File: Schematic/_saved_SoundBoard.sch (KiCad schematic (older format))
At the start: 0 parts

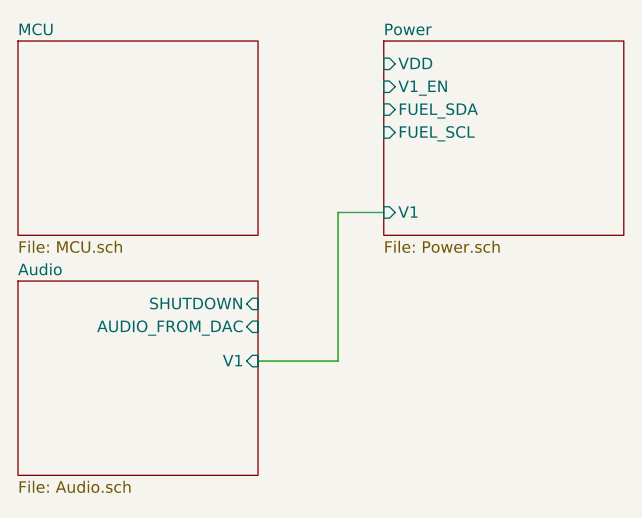
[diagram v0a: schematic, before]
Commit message: Add power circuitry
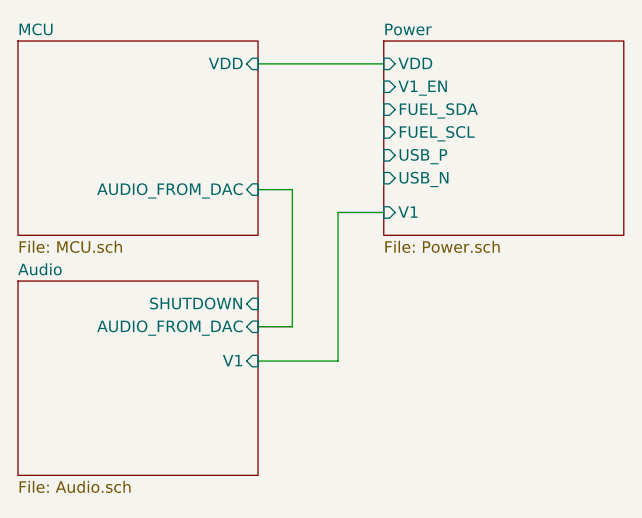
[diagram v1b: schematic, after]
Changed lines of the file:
@@
 F0 "MCU" 50
 F1 "MCU.sch" 50
+F2 "VDD" I R 2200 1250 50
+F3 "AUDIO_FROM_DAC" I R 2200 1800 50
 $EndSheet
 $Sheet
@@
 F5 "FUEL_SDA" I L 2750 1450 50
 F6 "FUEL_SCL" I L 2750 1550 50
+F7 "USB_P" I L 2750 1650 50
+F8 "USB_N" I L 2750 1750 50
 $EndSheet
 Wire Wire Line
@@
 Wire Wire Line
 	2550 1900 2750 1900
+Wire Wire Line
+	2200 1250 2750 1250
+Wire Wire Line
+	2200 1800 2350 1800
+Wire Wire Line
+	2350 1800 2350 2400
+Wire Wire Line
+	2350 2400 2200 2400
 $EndSCHEMATC
